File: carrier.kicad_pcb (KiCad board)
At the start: 4 copper layers, 20.3 x 68.6 mm, 30 parts, among them J1 Conn_01x26, J2 Conn_01x26, J3 Conn_02x06_Odd_Even, U1 CARAVEL, U2 LP5907MFX-1.8, U3 LP5907MFX-1.8, U4 LP5907MFX-3.3, U5 W25Q128JVS, U6 LP5907MFX-3.3, X1 SG-5032CAN

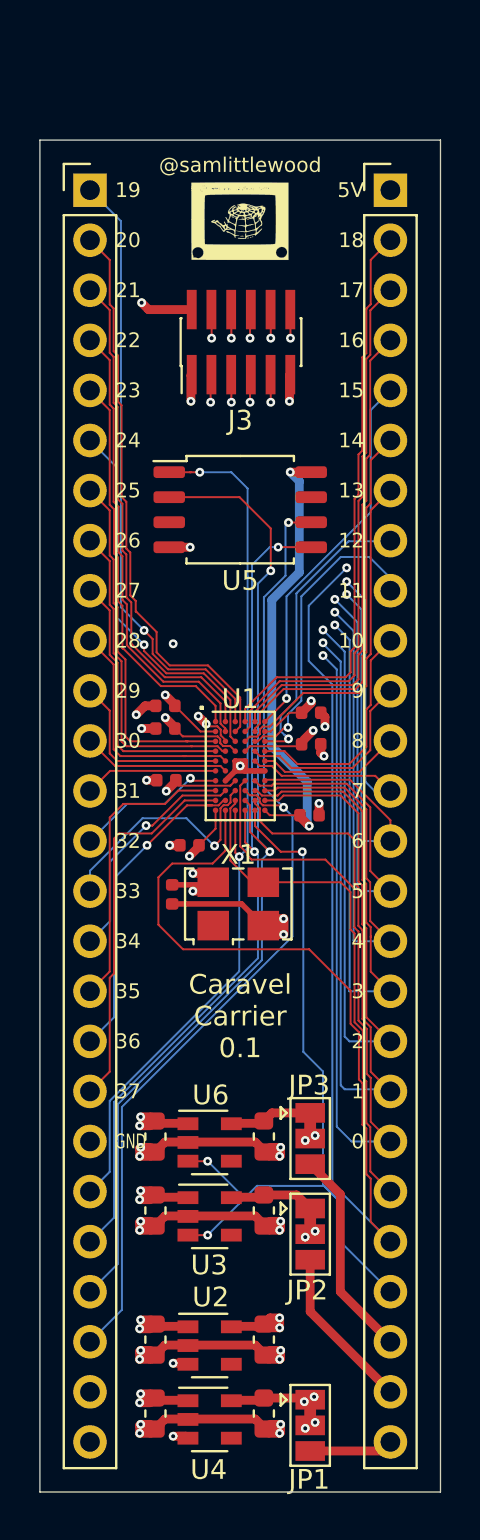
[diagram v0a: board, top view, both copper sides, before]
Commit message: Tidy up and ground pours.
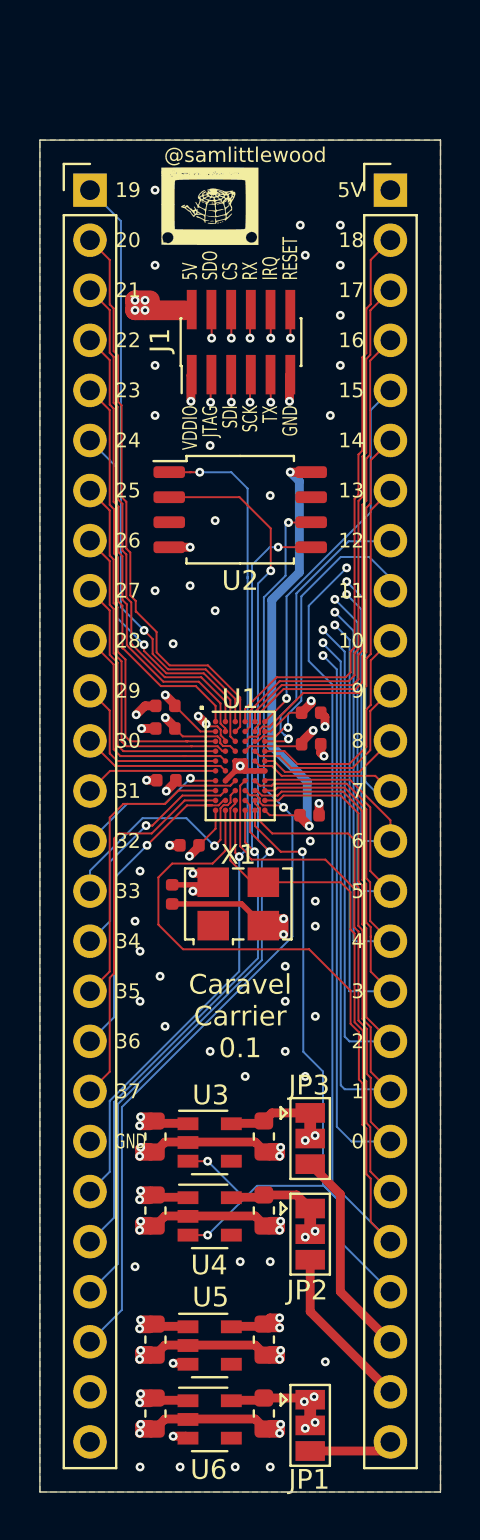
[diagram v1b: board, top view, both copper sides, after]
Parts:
- C1, C2, C5, C6: value C_Small -> 1u
- C10, C11, C12, C13, C14, C15, C9: value C_Small -> 22n
- C3, C4, C7, C8: value C_Small -> 4u7
- moved G*** 1.70 mm to (67.2, 51.6)
- renumbered J3 to J1, J1 to J2, J2 to J3, U5 to U2, U6 to U3, U3 to U4, U2 to U5, U4 to U6
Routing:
- net +5V: track 101.4 -> 103.8 mm, vias 11 -> 14
- net vccd1: track 43.8 -> 44.5 mm
- net vddio: track 70.9 -> 71.5 mm
- net vdda1: track 47.3 -> 47.9 mm
- net vdda: track 68.8 -> 69.4 mm
- net GND: vias 30 -> 71
- added copper zone on B.Cu, net GND
- added copper zone on F.Cu, net GND
- added copper zone on In2.Cu, net GND
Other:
- board text added: "CS"
- board text added: "IRQ"
- board text added: "JTAG"
- board text added: "RESET"
- board text added: "RX"
- board text added: "SCK"
- board text added: "SDI"
- board text added: "SDO"
- board text added: "TX"
- board text added: "VDDIO"

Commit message: Tidy up regulators.
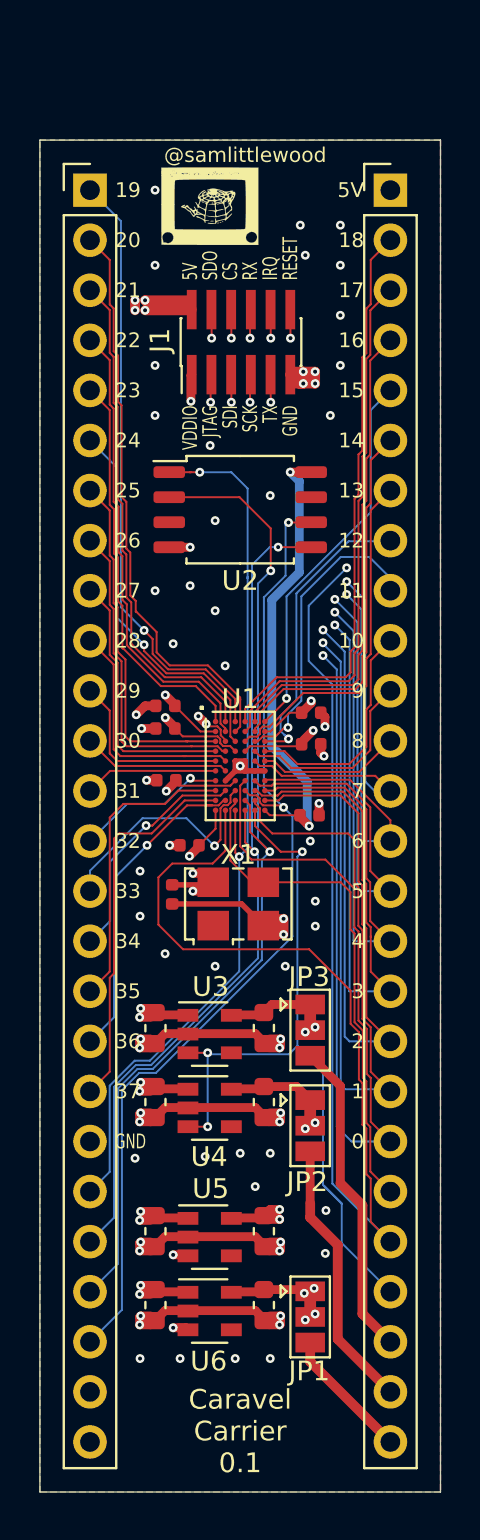
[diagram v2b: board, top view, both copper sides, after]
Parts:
- moved C1 5.50 mm to (64.4, 103.6)
- moved C2 5.50 mm to (64.4, 93.3)
- moved C3 5.50 mm to (69.9, 103.6)
- moved C4 5.50 mm to (69.9, 97.0)
- moved C5 5.50 mm to (64.4, 107.3)
- moved C6 5.50 mm to (64.4, 97.0)
- moved C7 5.50 mm to (69.9, 107.3)
- moved C8 5.50 mm to (69.9, 93.3)
- moved JP1 5.50 mm to (72.3, 108.0)
- moved JP2 5.50 mm to (72.3, 98.2)
- moved JP3 5.50 mm to (72.3, 93.4)
- moved U3 5.50 mm to (67.2, 93.6)
- moved U4 5.50 mm to (67.2, 97.3)
- moved U5 5.50 mm to (67.2, 103.9)
- moved U6 5.50 mm to (67.2, 107.7)
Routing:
- net vdda: track 69.4 -> 63.3 mm
- net vccd1: track 44.5 -> 39.0 mm
- net vddio: track 71.5 -> 66.0 mm
- net vdda1: track 47.9 -> 42.4 mm
- net ext_3v3: track 10.7 -> 16.2 mm
- net ext_1v8: track 8.39 -> 13.9 mm
- net vccd: track 33.7 -> 28.5 mm
- net GND: track 58.1 -> 62.2 mm, vias 71 -> 70
- net ext_vddio: track 4.26 -> 7.38 mm
- net gpio: track 41.2 -> 39.9 mm
- net +5V: track 103.8 -> 104.5 mm
- net flash_clk: track 50.5 -> 51.0 mm

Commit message: Flipped to have regulators at top, makes pin/io number a better match.
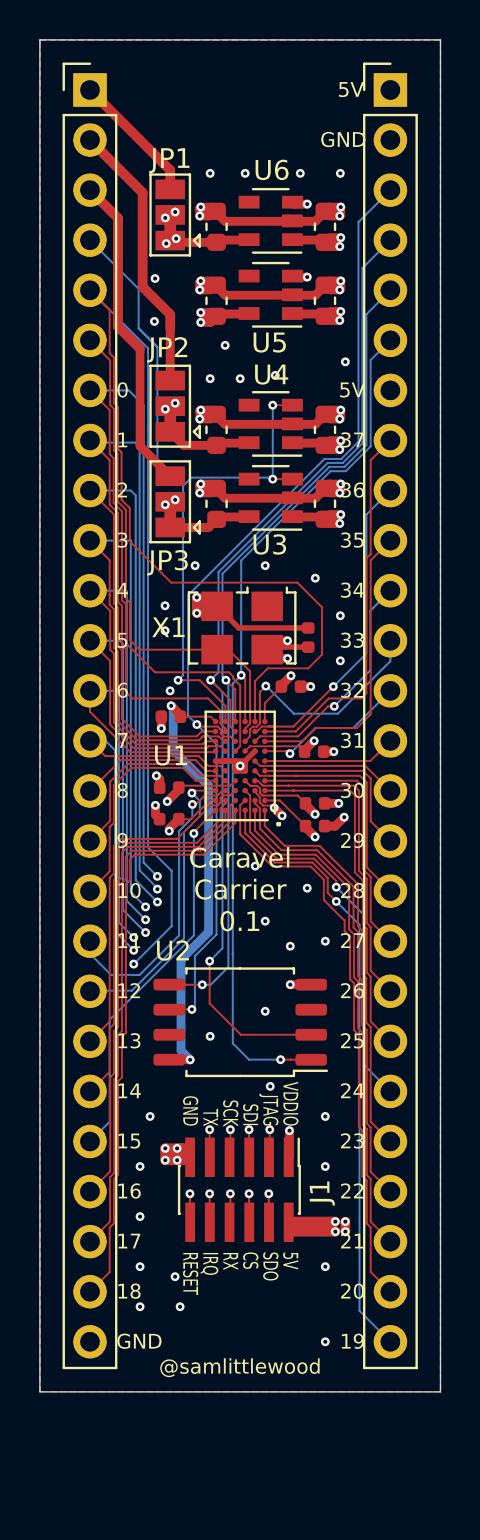
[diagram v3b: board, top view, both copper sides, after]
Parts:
- G***: moved to B.Cu
- moved JP1 56.3 mm to (65.2, 52.0), turned to 90 degrees
- moved U6 55.4 mm to (70.3, 52.4), turned to 180 degrees
- moved C5 55.4 mm to (73.0, 52.6), turned to 90 degrees
- moved C7 54.8 mm to (67.5, 52.6), turned to 90 degrees
- moved G*** 50.1 mm to (68.7, 101.6)
- moved C1 48.0 mm to (73.0, 56.4), turned to 90 degrees
- moved U5 47.9 mm to (70.3, 56.1), turned to 180 degrees
- moved C3 47.3 mm to (67.5, 56.4), turned to 90 degrees
- moved J1 43.0 mm to (68.7, 101.5), turned to 270 degrees
- moved JP2 37.2 mm to (65.2, 61.8), turned to 90 degrees
- moved C6 35.2 mm to (73.0, 63.0), turned to 90 degrees
- moved U4 34.8 mm to (70.3, 62.6), turned to 180 degrees
- moved C4 34.2 mm to (67.5, 63.0), turned to 90 degrees
- moved C2 28.0 mm to (73.0, 66.7), turned to 90 degrees
- moved JP3 27.7 mm to (65.2, 66.6), turned to 90 degrees
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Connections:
- J2 pad 1: mprj_io[19] -> ext_vddio
- J2 pad 10: mprj_io[28] -> mprj_io[3]
- J2 pad 11: mprj_io[29] -> mprj_io[4]
- J2 pad 12: mprj_io[30] -> mprj_io[5]
- J2 pad 13: mprj_io[31] -> mprj_io[6]
- J2 pad 14: mprj_io[32] -> mprj_io[7]
- J2 pad 15: mprj_io[33] -> mprj_io[8]
- J2 pad 16: mprj_io[34] -> mprj_io[9]
- J2 pad 17: mprj_io[35] -> mprj_io[10]
- J2 pad 18: mprj_io[36] -> mprj_io[11]
- J2 pad 19: mprj_io[37] -> mprj_io[12]
- J2 pad 2: mprj_io[20] -> ext_1v8
- J2 pad 20: GND -> mprj_io[13]
- J2 pad 21: flash_csb -> mprj_io[14]
- J2 pad 22: flash_io0 -> mprj_io[15]
- J2 pad 23: flash_io1 -> mprj_io[16]
- J2 pad 24: flash_clk -> mprj_io[17]
- J2 pad 25: Net-(J2-Pad25) -> mprj_io[18]
- J2 pad 3: mprj_io[21] -> ext_3v3
- J2 pad 4: mprj_io[22] -> gpio
- J2 pad 5: mprj_io[23] -> resetb
- J2 pad 6: mprj_io[24] -> clock
- J2 pad 7: mprj_io[25] -> mprj_io[0]
- J2 pad 8: mprj_io[26] -> mprj_io[1]
- J2 pad 9: mprj_io[27] -> mprj_io[2]
- J3 pad 10: mprj_io[10] -> mprj_io[35]
- J3 pad 11: mprj_io[9] -> mprj_io[34]
- J3 pad 12: mprj_io[8] -> mprj_io[33]
- J3 pad 13: mprj_io[7] -> mprj_io[32]
- J3 pad 14: mprj_io[6] -> mprj_io[31]
- J3 pad 15: mprj_io[5] -> mprj_io[30]
- J3 pad 16: mprj_io[4] -> mprj_io[29]
- J3 pad 17: mprj_io[3] -> mprj_io[28]
- J3 pad 18: mprj_io[2] -> mprj_io[27]
- J3 pad 19: mprj_io[1] -> mprj_io[26]
- J3 pad 2: mprj_io[18] -> GND
- J3 pad 20: mprj_io[0] -> mprj_io[25]
- J3 pad 21: clock -> mprj_io[24]
- J3 pad 22: resetb -> mprj_io[23]
- J3 pad 23: gpio -> mprj_io[22]
- J3 pad 24: ext_3v3 -> mprj_io[21]
- J3 pad 25: ext_1v8 -> mprj_io[20]
- J3 pad 26: ext_vddio -> mprj_io[19]
- J3 pad 3: mprj_io[17] -> flash_clk
- J3 pad 4: mprj_io[16] -> flash_io1
- J3 pad 5: mprj_io[15] -> flash_io0
- J3 pad 6: mprj_io[14] -> flash_csb
- J3 pad 7: mprj_io[13] -> +5V
- J3 pad 8: mprj_io[12] -> mprj_io[37]
- J3 pad 9: mprj_io[11] -> mprj_io[36]
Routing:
- net +5V: track 104.5 -> 98.4 mm
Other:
- board text removed: "n/c"

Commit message: Tidy up power routing.
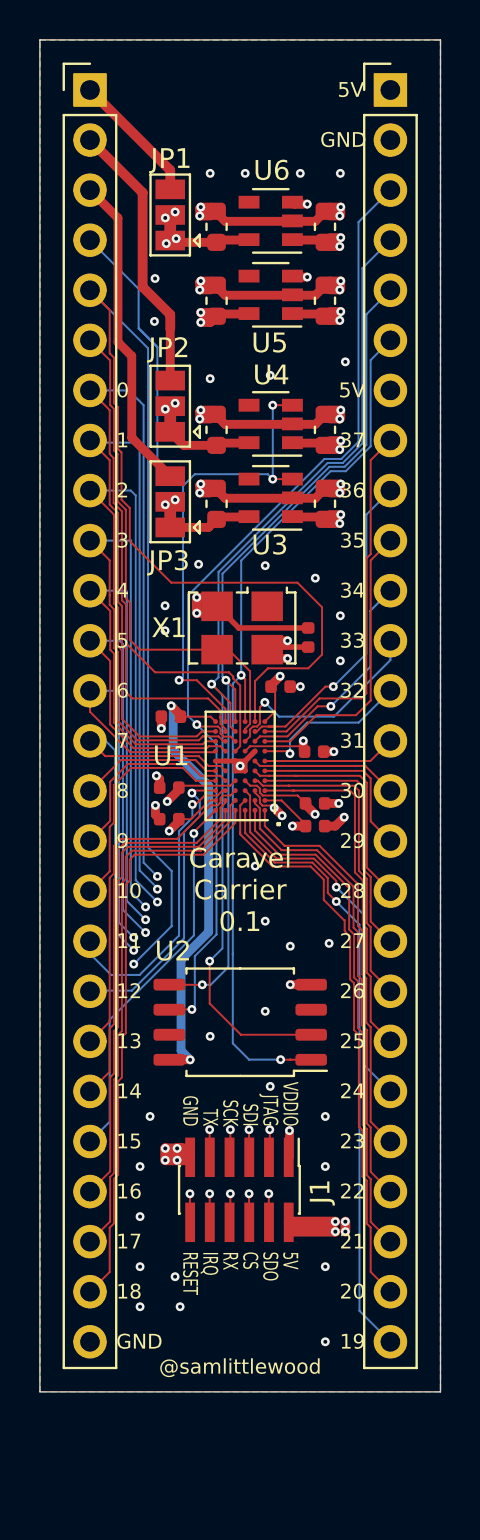
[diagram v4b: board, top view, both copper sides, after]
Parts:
- moved C11 0.53 mm to (70.8, 76.0)
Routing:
- net vdda: track 63.3 -> 75.8 mm
- net vddio: track 66.0 -> 56.4 mm, vias 5 -> 4
- net vdda1: track 42.4 -> 39.4 mm
- net vccd1: track 39.0 -> 36.5 mm
- net mprj_io[33]: track 12.4 -> 11.4 mm
- net vccd: track 28.5 -> 27.7 mm
- net GND: track 62.2 -> 61.7 mm, vias 70 -> 67
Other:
- net class Default: clearance 0.05 -> 0.1
- rule trace_clearance: 0.05 -> 0.1

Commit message: Tidy up oscillator.
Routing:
- net GND: track 61.7 -> 62.2 mm
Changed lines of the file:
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@@
     (thickness 1.6)
     (drawings 75)
-    (tracks 1055)
+    (tracks 1056)
     (zones 0)
     (modules 30)
@@
     (effects (font (size 0.75 0.75) (thickness 0.1)) (justify left))
   )
-  (gr_poly (pts (xy 66.93 72.8) (xy 71.33 72.8) (xy 71.33 73.2) (xy 66.93 73.2)) (layer F.Mask) (width 0.1))
+  (gr_poly (pts (xy 67.48 72.8) (xy 71.33 72.8) (xy 71.33 73.2) (xy 67.48 73.2)) (layer F.Mask) (width 0.1))
   (gr_line (start 78.89 43.17) (end 78.89 111.75) (layer Edge.Cuts) (width 0.05))
   (gr_line (start 58.57 43.17) (end 78.89 43.17) (layer Edge.Cuts) (width 0.05))
@@
   (segment (start 66.68 65.75) (end 66.73 65.7) (width 0.45) (layer F.Cu) (net 3))
   (segment (start 66.68 66.15) (end 66.68 65.75) (width 0.45) (layer F.Cu) (net 3))
-  (segment (start 68.6584 73) (end 67.5584 71.9) (width 0.28) (layer F.Cu) (net 3) (status 20))
-  (segment (start 72.18 73) (end 68.6584 73) (width 0.28) (layer F.Cu) (net 3) (status 10))
   (via (at 66.53 71.45) (size 0.45) (drill 0.2) (layers F.Cu B.Cu) (net 3))
   (via (at 66.53 72.25) (size 0.45) (drill 0.2) (layers F.Cu B.Cu) (net 3))
@@
   (segment (start 69.859999 82.009999) (end 69.73 81.88) (width 0.1) (layer F.Cu) (net 3))
   (segment (start 70.455 82.125) (end 70.339999 82.009999) (width 0.1) (layer F.Cu) (net 3))
+  (segment (start 67.73 72.0716) (end 67.5584 71.9) (width 0.28) (layer F.Cu) (net 3))
+  (segment (start 67.73 73) (end 67.73 72.0716) (width 0.28) (layer F.Cu) (net 3))
+  (segment (start 72.18 73) (end 67.73 73) (width 0.28) (layer F.Cu) (net 3))
   (via (at 74.064 103.622) (size 0.45) (drill 0.2) (layers F.Cu B.Cu) (net 4))
   (via (at 73.556 103.622) (size 0.45) (drill 0.2) (layers F.Cu B.Cu) (net 4))
@@
       )
     )
+  )
+  (zone (net 0) (net_name "") (layer F.Cu) (hatch edge 0.508)
+    (connect_pads (clearance 0.2))
+    (min_thickness 0.254)
+    (keepout (tracks allowed) (vias allowed) (copperpour not_allowed))
+    (fill (arc_segments 32) (thermal_gap 0.508) (thermal_bridge_width 0.508))
+    (polygon
+      (pts
+        (xy 72.73 72) (xy 72.73 75) (xy 66.73 75) (xy 66.73 70.5) (xy 71.23 70.5)
+      )
+    )

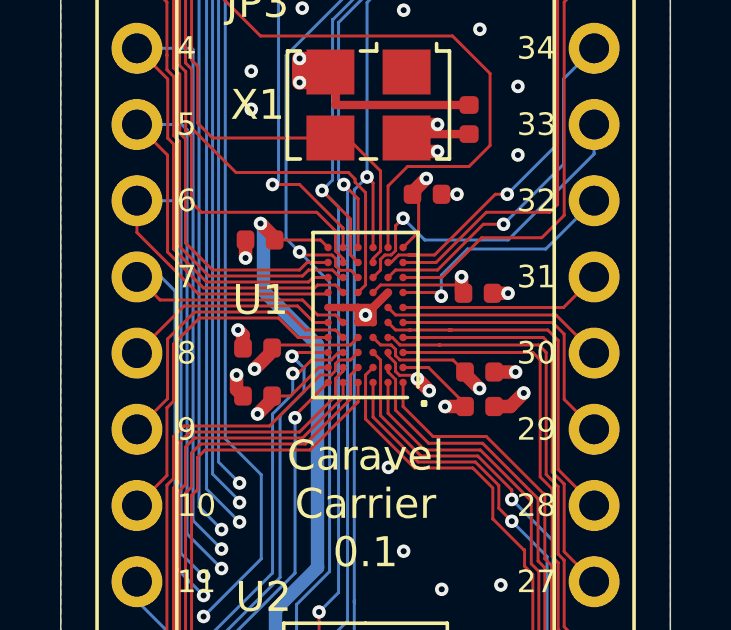
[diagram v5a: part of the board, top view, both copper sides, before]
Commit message: Solder mask clearance.
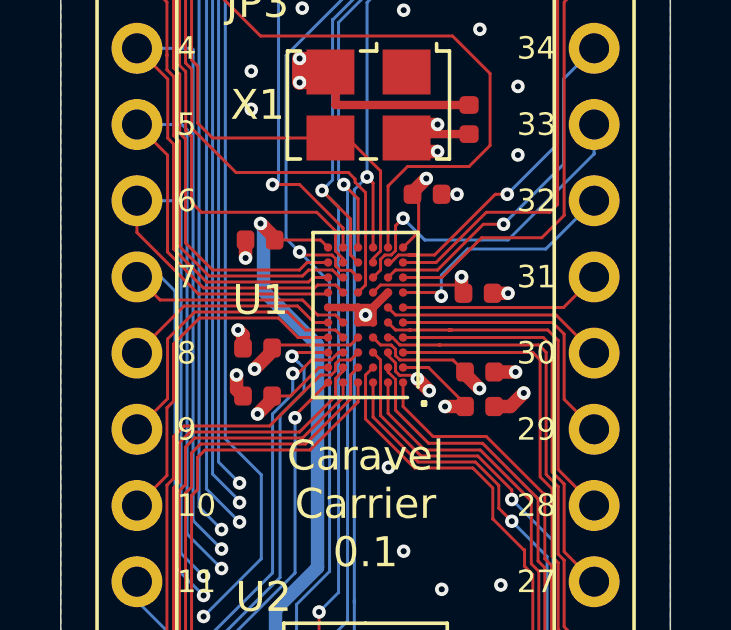
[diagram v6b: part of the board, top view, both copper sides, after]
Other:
- rule pad_to_mask_clearance: 0 -> 0.05

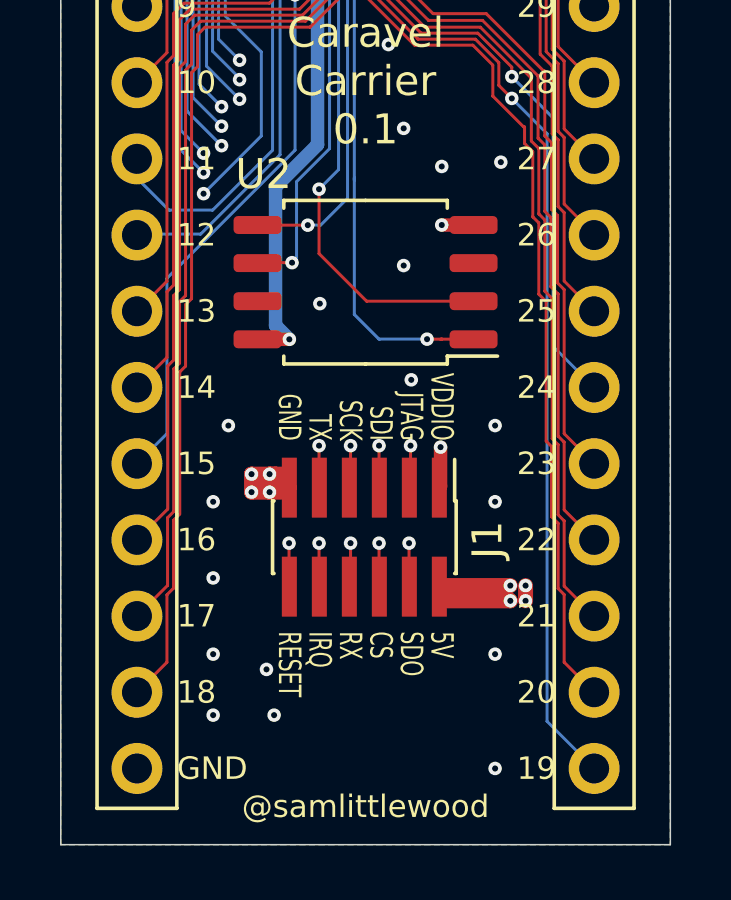
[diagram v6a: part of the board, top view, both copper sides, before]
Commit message: Use 1.27mm header.
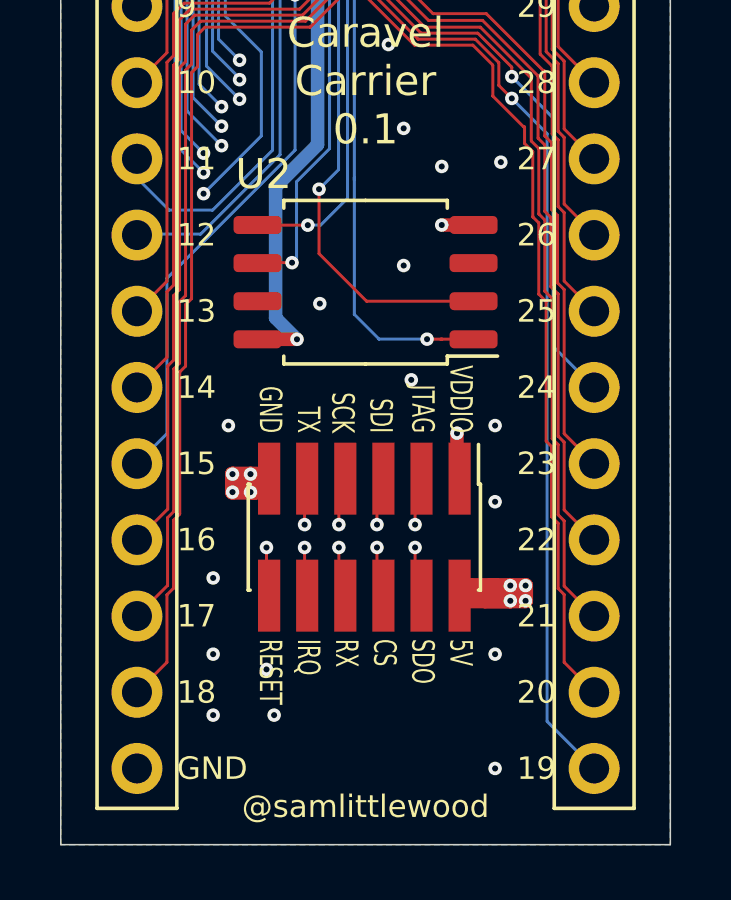
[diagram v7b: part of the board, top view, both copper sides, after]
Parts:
- J1: footprint Connector_PinHeader_1.00mm:PinHeader_2x06_P1.00mm_Vertical_SMD -> Connector_PinHeader_1.27mm:PinHeader_2x06_P1.27mm_Vertical_SMD
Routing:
- net mprj_io[6]: track 35.6 -> 37.9 mm
- net mprj_io[0]: track 68.5 -> 70.6 mm
- net mprj_io[2]: track 56.7 -> 58.7 mm
- net mprj_io[4]: track 46.4 -> 48.3 mm
- net +5V: track 98.4 -> 97.2 mm
- net GND: track 62.2 -> 61.0 mm, vias 67 -> 66
- net vddio: track 56.4 -> 55.9 mm
- net mprj_io[3]: track 55.8 -> 55.3 mm
